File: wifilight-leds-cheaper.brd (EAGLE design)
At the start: 50.8 x 50.8 mm, 49 parts, among them Q1 BUK98180-100A, Q2 BUK98180-100A, Q3 BUK98180-100A, Q4 BUK98180-100A, U2 PCA9685

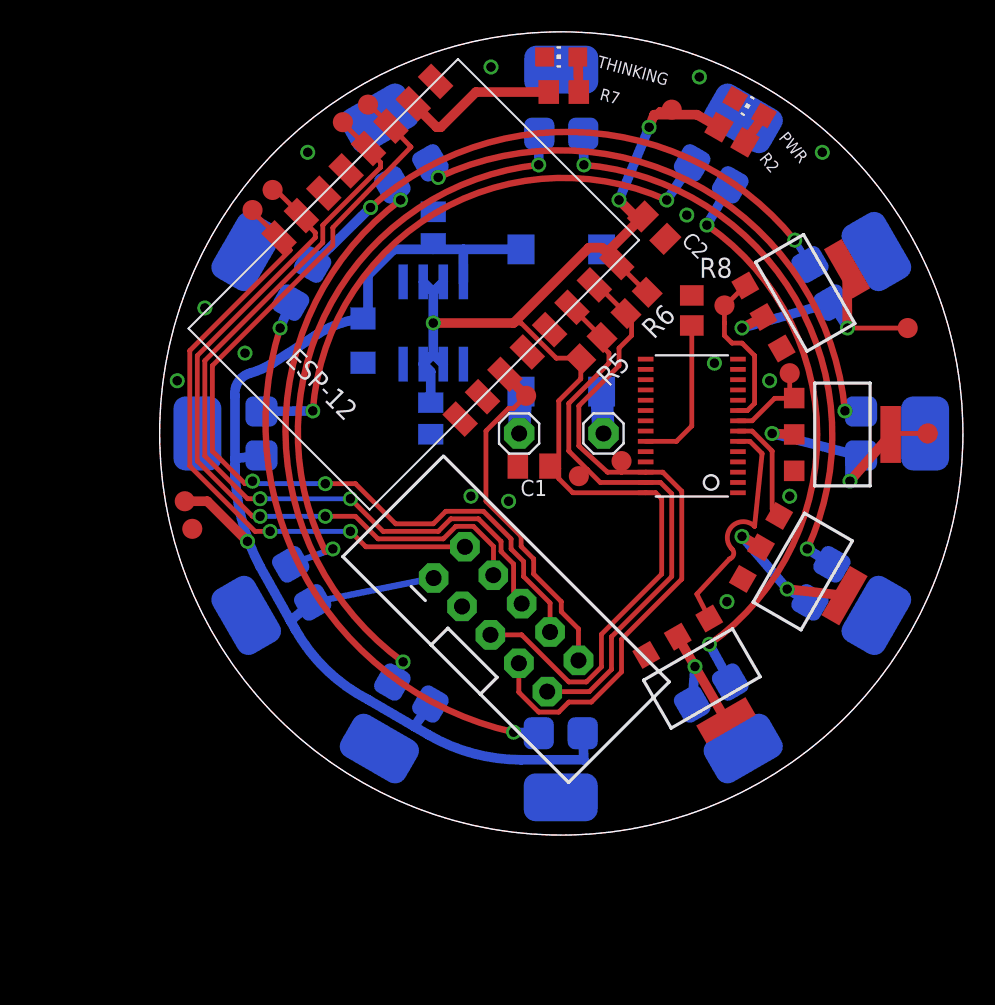
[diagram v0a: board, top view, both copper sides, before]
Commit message: Rotate socket to allow it not to clip through one of the SOT-223 transitors
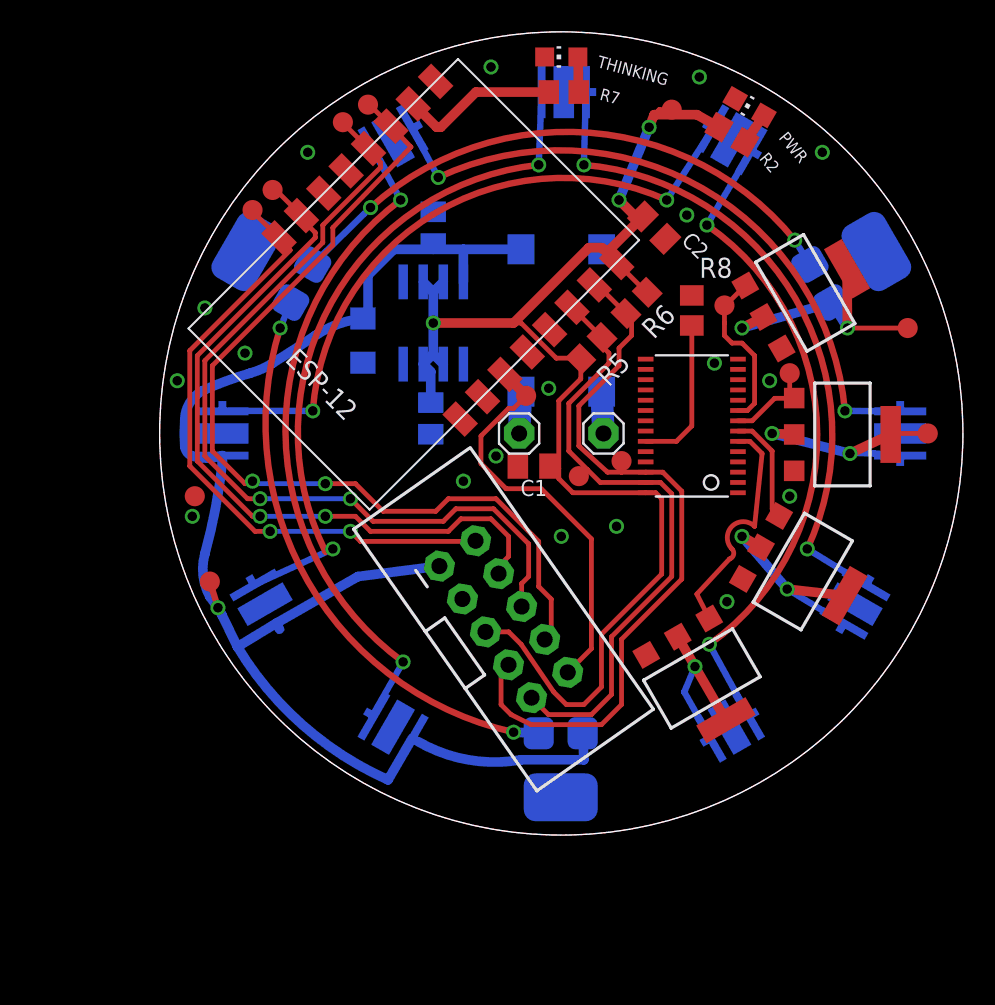
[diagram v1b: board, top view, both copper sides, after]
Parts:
- removed BL1, BL2, BL3, GL1, GL2, GL3, RL1, RL2, RL3: LUXEON-REBEL, SparkFun-LED:LUXEON-REBEL
- added LB1, LB2, LB3, LG1, LG2, LG3, LR1, LR2, LR3: XPEWHT-01-0000-00BC2, led:CREE_XLAMP
- moved TP12V 5.32 mm to (3.17, 16.0)
- moved TPGND 2.07 mm to (2.22, 21.4)
- moved JP2 0.16 mm to (21.7, 13.7), turned to 35 degrees
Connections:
- net 12V: now also LB3.A, LB3.A@1, LG3.A, LG3.A@1, LR3.A, LR3.A@1; no longer BL3.ANODE, GL3.ANODE, RL3.ANODE
- net B1: now also LB2.A, LB2.A@1, LB3.C, LB3.C@1; no longer BL2.ANODE, BL3.CATHODE
- net B2: now also LB1.A, LB1.A@1, LB2.C, LB2.C@1; no longer BL1.ANODE, BL2.CATHODE
- net G1: now also LG2.A, LG2.A@1, LG3.C, LG3.C@1; no longer GL2.ANODE, GL3.CATHODE
- net G2: now also LG1.A, LG1.A@1, LG2.C, LG2.C@1; no longer GL1.ANODE, GL2.CATHODE
- net GND: no longer BL1.P$3, BL2.P$3, BL3.P$3, GL1.P$3, GL2.P$3, GL3.P$3, RL1.P$3, RL2.P$3, RL3.P$3
- net P_BLUE: now also LB1.C, LB1.C@1; no longer BL1.CATHODE
- net P_GREEN: now also LG1.C, LG1.C@1; no longer GL1.CATHODE
- net P_RED: now also LR1.C, LR1.C@1; no longer RL1.CATHODE
- net R1: now also LR2.A, LR2.A@1, LR3.C, LR3.C@1; no longer RL2.ANODE, RL3.CATHODE
- net R2: now also LR1.A, LR1.A@1, LR2.C, LR2.C@1; no longer RL1.ANODE, RL2.CATHODE
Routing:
- net 12V: track 84.4 -> 91.1 mm
- net G1: track 33.2 -> 39.4 mm
- net R1: track 31.8 -> 37.8 mm
- net G2: track 31.9 -> 37.9 mm
- net B1: track 32.1 -> 38.0 mm
- net B2: track 32.2 -> 38.0 mm
- net R2: track 31.7 -> 37.5 mm
- net SCL: track 43.9 -> 47.3 mm
- net CH_PD: track 22.3 -> 25.6 mm
- net P_BLUE: track 8.48 -> 11.6 mm
- net SDA: track 36.8 -> 39.8 mm
- net P_GREEN: track 11.1 -> 14.0 mm
- net 3.3V: track 85.3 -> 88.0 mm
- net GPIO2: track 57.3 -> 58.9 mm
- net GPIO0: track 52.8 -> 54.3 mm
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
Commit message: Adding more signals to a better connector, moved THINKING LED to another GPIO due to conflict
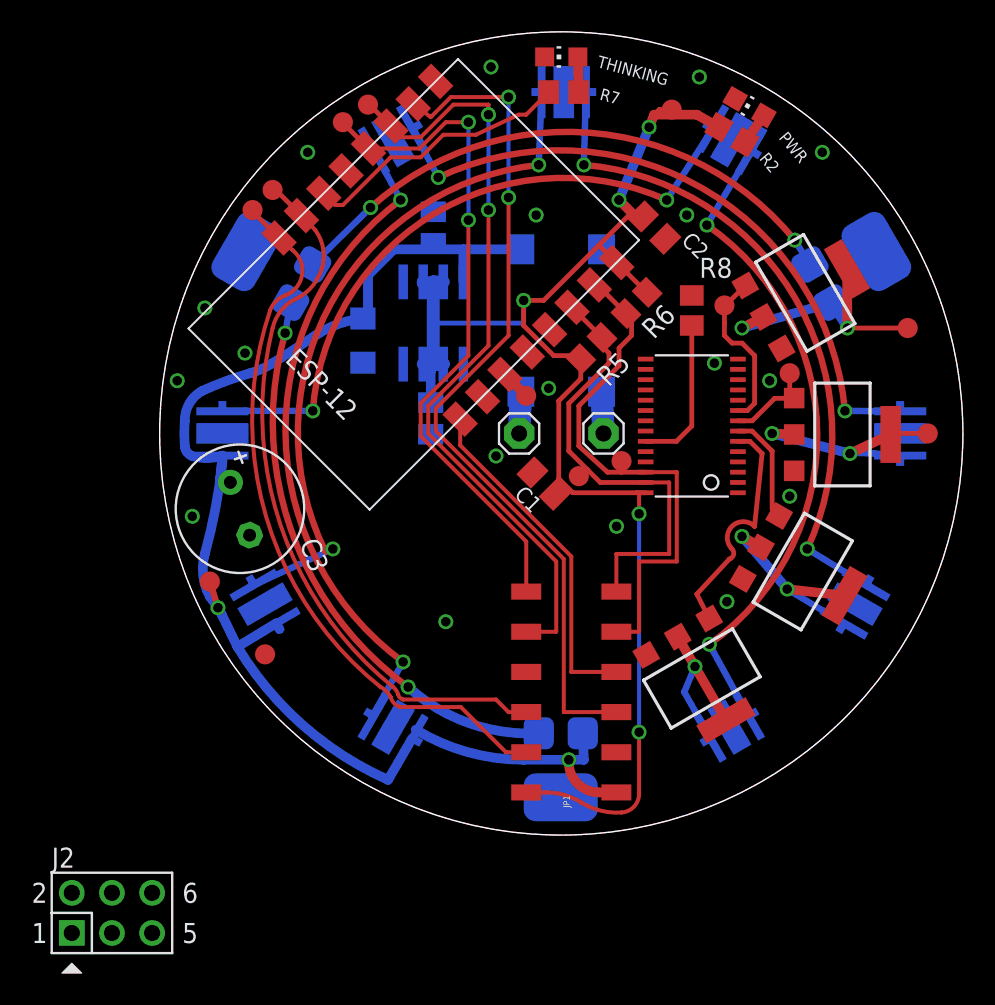
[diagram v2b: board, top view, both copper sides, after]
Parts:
- removed JP2: (no value), SparkFun-Connectors:2X5-SHROUDED_LOCK
- added C3: (no value), rcl:E3,5-8
- added J2: CON_HEADER_PRG_AVR_ICSP-PTH, dp_devices:HEADER_PRG_2X03
- added JP1: (no value), SparkFun-Connectors:2X6_SMD
- moved TPGND 10.9 mm to (6.67, 11.4)
- moved C1 1.28 mm to (24.3, 22.2), turned to 135 degrees
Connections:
- removed net DISCO: MPU.6
- new net GPIO15: JP1.5, MPU.2
- new net NA: JP1.8
- net 12V: now also C3.+, JP1.1; no longer JP2.1
- net 3.3V: now also JP1.2; no longer JP2.5
- net CH_PD: no longer JP2.10
- net GND: now also C3.-, JP1.3; no longer JP2.3
- net GPIO0: now also JP1.12; no longer JP2.6
- net GPIO2: now also JP1.10; no longer JP2.8
- net RESET: now also JP1.7
- net RXD: now also JP1.6; no longer JP2.4
- net SCL: now also JP1.9; no longer JP2.7
- net SDA: now also JP1.11; no longer JP2.9
- net THINKING: now also MPU.6; no longer MPU.2
- net TXD: now also JP1.4; no longer JP2.2
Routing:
- net GPIO15: track 0.00 -> 54.3 mm, vias 0 -> 2
- net CH_PD: track 25.6 -> 1.91 mm
- net RESET: track 0.00 -> 21.8 mm
- net SCL: track 47.3 -> 34.1 mm
- net GPIO0: track 54.3 -> 43.0 mm
- net SDA: track 39.8 -> 29.2 mm
- net GPIO2: track 58.9 -> 49.5 mm
- net THINKING: track 10.1 -> 17.3 mm
- net 3.3V: track 88.0 -> 93.3 mm, vias 3 -> 5
- net 12V: track 91.1 -> 87.1 mm, vias 1 -> 2
- net TXD: track 39.9 -> 43.6 mm, vias 2 -> 0
- net RXD: track 46.4 -> 44.1 mm, vias 2 -> 0
- net W1: track 32.8 -> 34.4 mm

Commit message: Added 3x4 pin headers. Added 2x i2c JST connectors.
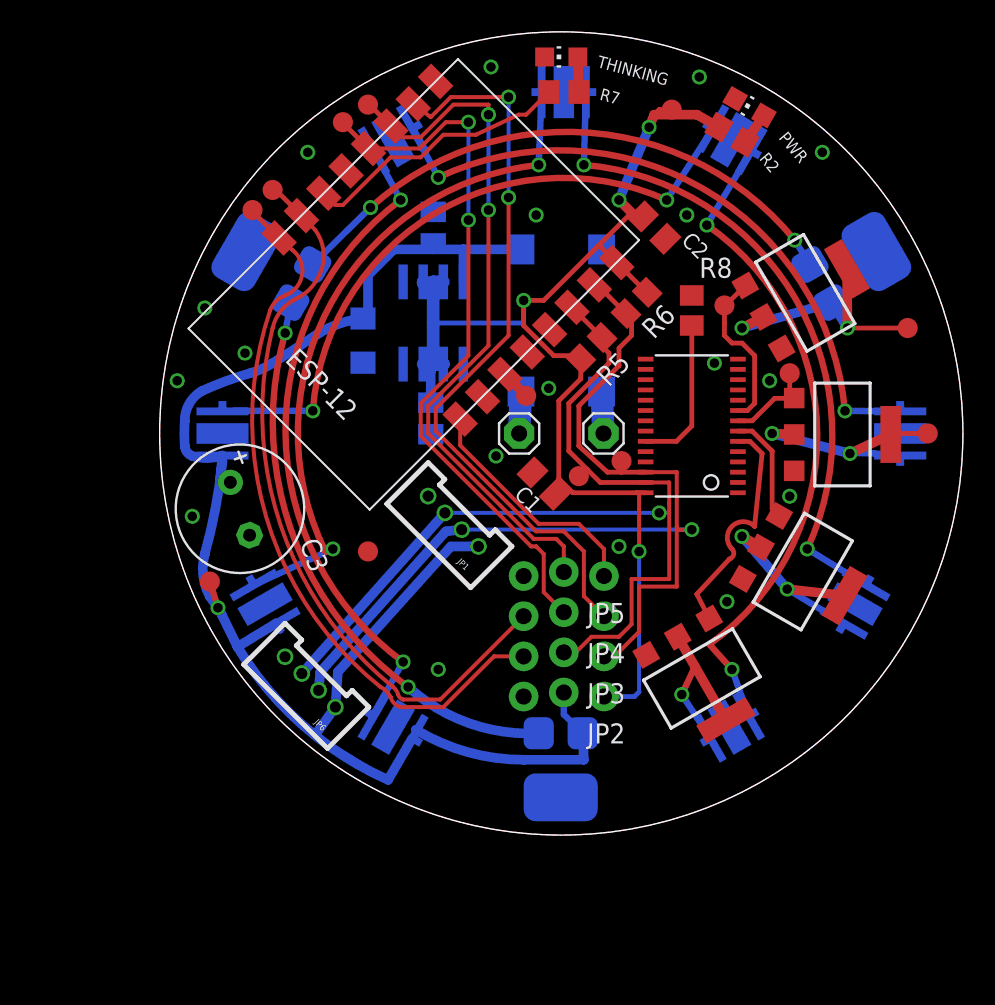
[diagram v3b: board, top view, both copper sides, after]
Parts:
- removed J2: CON_HEADER_PRG_AVR_ICSP-PTH, dp_devices:HEADER_PRG_2X03
- added JP2, JP3, JP4, JP5: (no value), SparkFun-Connectors:1X03_LOCK_NO_SILK
- added JP6: (no value), SparkFun-Connectors:1X04-1.5MM_JST
- JP1: device SparkFun-Connectors:2X6_SMD -> SparkFun-Connectors:1X04-1.5MM_JST
- moved JP1 12.0 mm to (20.2, 18.3), turned to 135 degrees
- moved TPGND 9.20 mm to (13.2, 17.9)
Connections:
- removed net NA: JP1.8
- net 12V: now also JP2.2, JP6.1
- net 3.3V: now also JP2.1; no longer JP1.2
- net GND: now also JP1.4, JP2.3, JP5.3, JP6.4; no longer JP1.3
- net GPIO0: now also JP4.2; no longer JP1.12
- net GPIO15: now also JP4.1; no longer JP1.5
- net GPIO2: now also JP5.2; no longer JP1.10
- net RESET: now also JP5.1; no longer JP1.7
- net RXD: now also JP4.3; no longer JP1.6
- net SCL: now also JP1.2, JP3.1, JP6.2; no longer JP1.9
- net SDA: now also JP1.3, JP3.2, JP6.3; no longer JP1.11
- net TXD: now also JP3.3; no longer JP1.4
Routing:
- net SDA: track 29.2 -> 63.2 mm, vias 0 -> 1
- net SCL: track 34.1 -> 65.1 mm, vias 0 -> 1
- net 12V: track 87.1 -> 108.5 mm, vias 2 -> 1
- net 3.3V: track 93.3 -> 81.4 mm, vias 5 -> 4
- net GPIO15: track 54.3 -> 47.0 mm
- net RESET: track 21.8 -> 15.2 mm
- net GPIO2: track 49.5 -> 44.9 mm
- net GPIO0: track 43.0 -> 45.5 mm
- net RXD: track 44.1 -> 45.8 mm

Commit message: Mk6 complete & DRC'd
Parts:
- removed A, B: (no value), adafruit:1X01
- removed JP1, JP6: (no value), SparkFun-Connectors:1X04-1.5MM_JST
- removed JP2, JP3, JP4, JP5: (no value), SparkFun-Connectors:1X03_LOCK_NO_SILK
- removed LB1, LB2, LB3, LG1, LG2, LG3, LR1, LR2, LR3: XPEWHT-01-0000-00BC2, led:CREE_XLAMP
- removed P_RED, P_WHITE, RED, SCL, SDA, TP12V, TP3.3V, TPCHPD, TPGND, TPGPIO0, TPGPIO2, TPRX, TPTX, WHITE: TEST-POINT3X5, SparkFun-Passives:PAD.03X.05
- removed U2: PCA9685, adafruit:TSSOP28
- added CN1: (no value), adafruit:JST-PH-2-THM
- added LED1, LED2, LED3, LED4, LED5, LED6: RGBLED5050, adafruit:RGBLED5050
- added R10, R11, R12, R13: 10k, SparkFun-Resistors:1206
- added U$2: (no value), SparkFun-Aesthetics:OSHW-LOGO-S
- added U1: TCA6507PW, Texas Instruments_By_element14_Batch_1:SOP65P640X120-14N
- added X1: 53261-06, con-molex:53261-06
- C1, C2, C6, C7: device resistor:C0805K -> SparkFun-Passives:1206
- R2, R7: value ??? -> 220ohm; device resistor:R0805 -> SparkFun-Passives:1206
- R5, R6, R8: device resistor:R0805 -> SparkFun-Passives:1206
- moved WL2 39.4 mm to (44.8, 26.2), flipped to the top, turned to 90 degrees
- moved C3 34.4 mm to (39.4, 17.5), flipped to the bottom, turned to 0 degrees
- moved Q3 31.8 mm to (11.4, 25.4), turned to 90 degrees
- moved Q4 30.2 mm to (15.2, 33.0), turned to 90 degrees
- moved WL1 29.6 mm to (15.2, 43.0), flipped to the top, turned to 210 degrees
- moved C5 25.2 mm to (35.9, 21.0), flipped to the top
- moved Q2 20.6 mm to (15.2, 17.8), turned to 90 degrees
- moved Q1 18.7 mm to (22.5, 38.4), turned to 0 degrees
- moved C2 18.6 mm to (13.0, 34.9), flipped to the bottom, turned to 0 degrees
- moved C6 18.1 mm to (29.2, 24.8), flipped to the top, turned to 0 degrees
- moved B2 15.7 mm to (29.8, 17.5), flipped to the top
- moved REG2 13.0 mm to (22.9, 20.6), flipped to the top
- moved MPU 12.9 mm to (17.5, 39.1), flipped to the bottom, turned to 180 degrees
- moved R7 12.5 mm to (27.3, 34.6), turned to 90 degrees
- moved C7 12.1 mm to (29.2, 27.3), flipped to the top, turned to 0 degrees
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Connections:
- net N$25 renamed GPIO14
- net N$26 renamed GPIO16
- net N$28 renamed ADC
- removed net #OE: R8.2, U2.23
- removed net B1: LB2.A, LB2.A@1, LB3.C, LB3.C@1
- removed net B2: LB1.A, LB1.A@1, LB2.C, LB2.C@1
- removed net G1: LG2.A, LG2.A@1, LG3.C, LG3.C@1
- removed net G2: LG1.A, LG1.A@1, LG2.C, LG2.C@1
- removed net N$18: A.1, B2.AC1
- removed net N$19: B.1, B2.AC2
- removed net N$36: MPU.5
- removed net R1: LR2.A, LR2.A@1, LR3.C, LR3.C@1
- removed net R2: LR1.A, LR1.A@1, LR2.C, LR2.C@1
- new net AC1: B2.AC1, CN1.1
- new net AC2: B2.AC2, CN1.2
- new net EN: R8.2, U1.4
- new net GPIO12: MPU.14
- new net GPIO13: MPU.15
- new net N$30: LED2.5, LED3.2
- new net N$31: LED2.6, LED3.1
- new net N$32: LED2.4, LED3.3
- new net N$33: LED1.5, LED2.2
- new net N$34: LED1.6, LED2.1
- new net N$35: LED1.4, LED2.3
- new net N$37: LED4.5, LED5.2
- new net N$38: LED4.6, LED5.1
- new net N$39: LED4.4, LED5.3
- new net N$40: LED5.5, LED6.2
- new net N$41: LED5.6, LED6.1
- new net N$42: LED5.4, LED6.3
- new net N$6: U1.10
- new net POWERED: R2.1, U1.8
- net 12V: now also LED1.1, LED1.2, LED1.3, LED4.1, LED4.2, LED4.3, X1.6; no longer JP1.1, JP2.2, JP6.1, LB3.A, LB3.A@1, LG3.A, LG3.A@1, LR3.A, LR3.A@1, TP12V.P$1
- net 3.3V: now also R10.1, R11.1, R12.1, R8.1, U1.1; no longer JP2.1, R2.1, TP3.3V.P$1, U2.28
- net BLUE: now also U1.12; no longer U2.6
- net CH_PD: now also R11.2; no longer TPCHPD.P$1
- net GND: now also R13.1, U1.5, U1.6, U1.7, X1.5; no longer JP1.4, JP2.3, JP5.3, JP6.4, R8.1, TPGND.P$1, U2.14, U2.25
- net GPIO0: now also R12.2, X1.4; no longer JP4.2, TPGPIO0.P$1
- net GPIO15: now also R13.2; no longer JP4.1
- net GPIO2: no longer JP5.2, TPGPIO2.P$1
- net GREEN: now also U1.14; no longer U2.7
- net P_BLUE: now also LED3.4, LED6.4; no longer LB1.C, LB1.C@1
- net P_GREEN: now also LED3.6, LED6.6; no longer LG1.C, LG1.C@1
- net P_RED: now also LED3.5, LED6.5; no longer LR1.C, LR1.C@1, P_RED.P$1
- net P_WHITE: no longer P_WHITE.P$1
- net RED: now also U1.13; no longer RED.P$1, U2.8
- net RESET: now also R10.2, X1.3; no longer JP5.1
- net RXD: now also X1.2; no longer JP4.3, TPRX.P$1
- net SCL: now also MPU.5, U1.2; no longer JP1.2, JP3.1, JP6.2, MPU.15, SCL.P$1, U2.26
- net SDA: now also MPU.6, U1.3; no longer JP1.3, JP3.2, JP6.3, MPU.14, SDA.P$1, U2.27
- net THINKING: now also U1.9; no longer MPU.6
- net TXD: now also X1.1; no longer JP3.3, TPTX.P$1
- net WHITE: now also U1.11; no longer U2.9, WHITE.P$1
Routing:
- net 3.3V: track 81.4 -> 134.5 mm, vias 4 -> 1
- net RESET: track 15.2 -> 63.4 mm
- net GPIO2: track 44.9 -> 0.00 mm, vias 2 -> 0
- net GPIO15: track 47.0 -> 3.35 mm, vias 2 -> 0
- net G1: track 39.4 -> 0.00 mm, vias 2 -> 0
- net B2: track 38.1 -> 0.00 mm, vias 2 -> 0
- net B1: track 38.0 -> 0.00 mm, vias 2 -> 0
- net G2: track 37.9 -> 0.00 mm, vias 2 -> 0
- net R1: track 37.8 -> 0.00 mm, vias 2 -> 0
- net R2: track 37.5 -> 0.00 mm, vias 2 -> 0
- net P_BLUE: track 11.8 -> 43.7 mm, vias 1 -> 0
- net TXD: track 43.6 -> 14.7 mm
- net N$42: track 0.00 -> 26.6 mm, vias 0 -> 2
- net N$31: track 0.00 -> 26.0 mm, vias 0 -> 2
- net N$40: track 0.00 -> 24.0 mm, vias 0 -> 2
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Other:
- board size 50.8 x 50.8 mm -> 48.3 x 48.3 mm
- board text added: "WifiLight"
- board text added: "mk6"
